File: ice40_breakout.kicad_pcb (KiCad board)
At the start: 4 copper layers, 80 x 100 mm, 224 parts, among them J1 Conn_01x10, J2 Conn_01x08, J3 Conn_01x06, J4 Conn_01x08, J5 USB_B_Micro, J6 7-17 V IN, Q1 2N7002, Q1 DMP3099L-7, SW1 SW_Push, SW2 SW_Push, SW3 SW_Push, SW4 SW_Push, SW5 SW_Push, SW6 SW_Push, SW7 JS202011SCQN, SW8 JS202011SCQN, SW9 JS202011SCQN, U1 ICE40HX4K-TQ144, U10 MAX40200AUK, U11 TXS0108EPW, U12 MAX40200AUK, U12 TPS562201, U13 TXS0108EPW, U14 MIC5365-3.3YC5, U15 MAX40200AUK, U2 IS61WV5128EDBLL-10TLI, U3 93LCxxBT-I_OT, U4 FT2232H, U5 IS25LP080D, U6 TLV62568APDRLR, U7 TLV62568APDRLR, U8 TXS0108EPW, U9 TXS0108EPW, Y1 ECS-3225S33-120-FN-TR, Y2 ECS-3225S33-500-FN-TR

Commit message: Continued on Power PCB design
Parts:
- moved C2 112.4 mm to (128.5, 63.6), turned to 90 degrees
- moved R14 103.2 mm to (127.0, 63.6), turned to 90 degrees
- moved R15 101.7 mm to (125.5, 63.6), turned to 270 degrees
- moved U6 95.4 mm to (123.5, 63.5), turned to 270 degrees
- moved C4 49.4 mm to (123.5, 67.8)
- moved C3 46.5 mm to (123.5, 66.2)
- moved C1 46.1 mm to (123.5, 61.2)
- moved L1 42.6 mm to (120.5, 65.2), turned to 270 degrees
- moved L2 26.6 mm to (126.2, 56.5), turned to 0 degrees
- moved C5 24.6 mm to (122.2, 53.5), turned to 90 degrees
- moved U7 23.3 mm to (124.5, 53.5), turned to 0 degrees
- moved C7 22.2 mm to (127.2, 53.5), turned to 90 degrees
- moved C8 21.9 mm to (128.8, 53.5), turned to 90 degrees
- moved R17 20.6 mm to (124.6, 51.5), turned to 0 degrees
- moved R16 18.7 mm to (124.6, 50.0), turned to 180 degrees
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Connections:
- net Net-(C34-Pad1) renamed /power/V_IN_FILTERED
- net Net-(C34-Pad2) renamed /power/GND_IN_FILTERED
- net Net-(C36-Pad1) renamed /power/V_IN_CHOKE
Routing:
- net /power/5V_IN: track 0.00 -> 27.6 mm
- net /power/V_IN_CHOKE: track 0.00 -> 11.5 mm
- net /power/V_IN: track 0.00 -> 8.98 mm
- net /power/GND_IN: track 0.00 -> 8.95 mm
- net +1V2: track 0.00 -> 8.01 mm, vias 0 -> 2
- net Net-(C43-Pad1): track 0.00 -> 6.06 mm
- net /power/FB_5V: track 0.05 -> 5.61 mm
- net /power/FB_1V2: track 0.00 -> 4.53 mm
- net Net-(C43-Pad2): track 0.00 -> 2.05 mm
- net GND: track 0.85 -> 2.85 mm, vias 11 -> 27
- net PG: track 1.10 -> 2.22 mm, vias 1 -> 2
- net /power/EN_HIGH_VOLTAGE: track 0.00 -> 1.05 mm, vias 0 -> 1
- net /power/EN_LOW_VOLTAGE: track 0.75 -> 1.50 mm, vias 1 -> 2
- net /power/V_IN_FILTERED: vias 0 -> 3
- net /power/GND_IN_FILTERED: vias 0 -> 3
- added copper zone on F.Cu, net +1V2
- added copper zone on F.Cu, net /power/5V_IN
- added copper zone on B.Cu, net /power/GND_IN_FILTERED
- added copper zone on F.Cu, net /power/GND_IN_FILTERED
- added copper zone on B.Cu, net /power/V_IN_FILTERED
- added copper zone on F.Cu, net /power/V_IN_FILTERED
- added copper zone on F.Cu, net /power/V_IN_PROTECTED
- added copper zone on F.Cu, net Net-(C43-Pad1)
- added copper zone on F.Cu, net Net-(L1-Pad1)
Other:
- net class V_IN added: clearance 0.2, trace_width 1, via_dia 0.6, via_drill 0.3

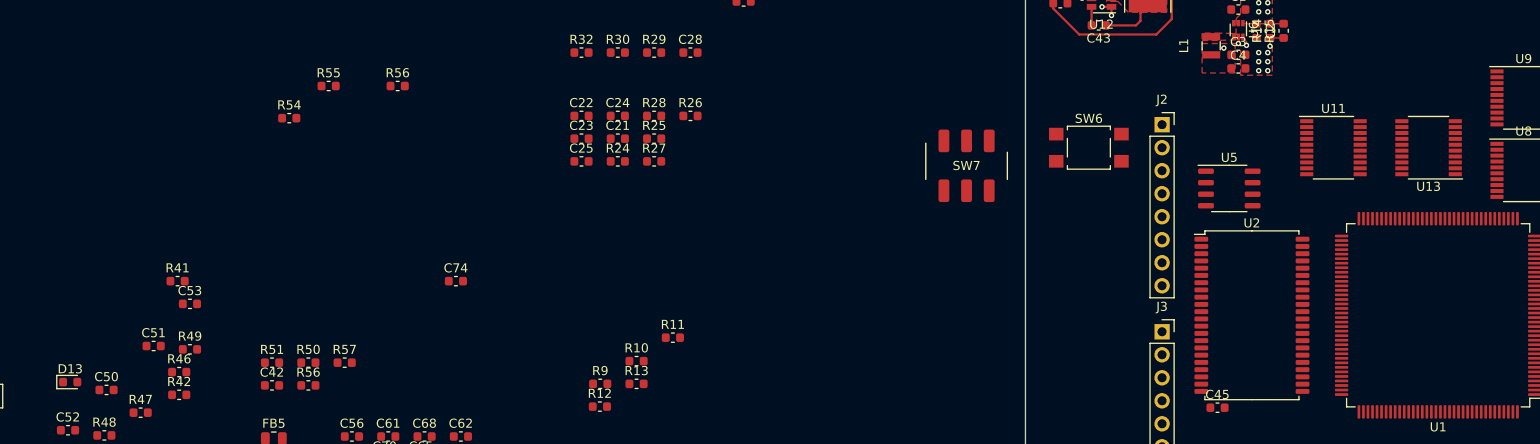
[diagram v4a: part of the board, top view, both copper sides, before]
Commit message: Implemented proper Powerseparation between FTDI and FPGA. The old solution may not work correctly
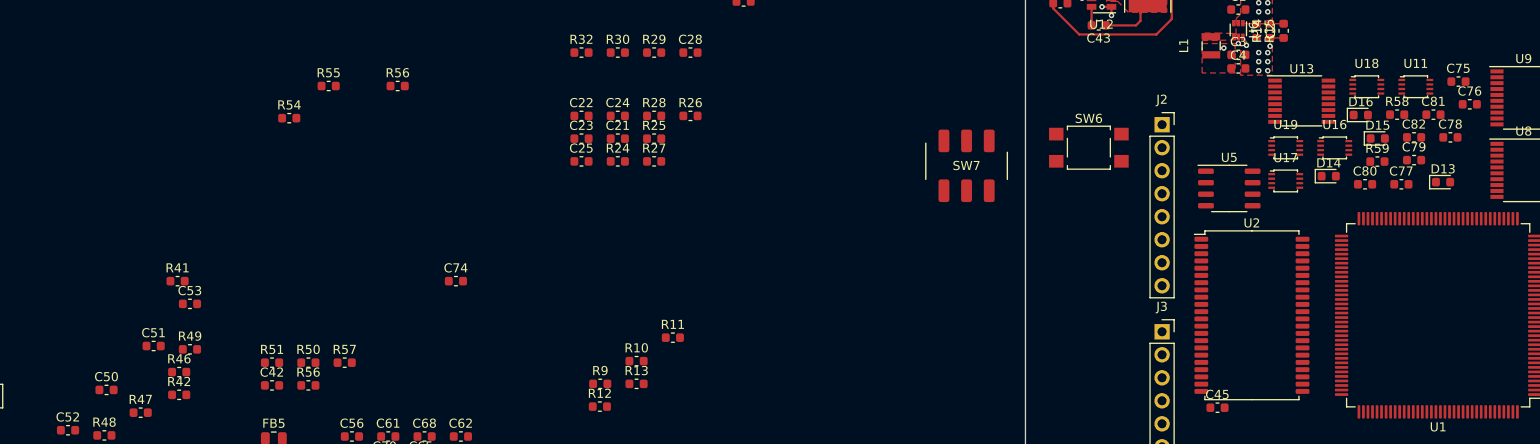
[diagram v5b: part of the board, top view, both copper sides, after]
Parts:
- added C75: 100nF, Capacitor_SMD:C_0603_1608Metric, F.Cu at (147.8, 69.2)
- added C76: 100nF, Capacitor_SMD:C_0603_1608Metric, F.Cu at (149.1, 71.7)
- added C77: 100nF, Capacitor_SMD:C_0603_1608Metric, F.Cu at (141.5, 80.5)
- added C78: 100nF, Capacitor_SMD:C_0603_1608Metric, F.Cu at (146.9, 75.4)
- added C79: 100nF, Capacitor_SMD:C_0603_1608Metric, F.Cu at (142.9, 77.9)
- added C80: 100nF, Capacitor_SMD:C_0603_1608Metric, F.Cu at (137.5, 80.5)
- added C81: 100nF, Capacitor_SMD:C_0603_1608Metric, F.Cu at (145.0, 72.8)
- added C82: 100nF, Capacitor_SMD:C_0603_1608Metric, F.Cu at (142.9, 75.4)
- added D14: CDBU5020, Diode_SMD:D_0603_1608Metric, F.Cu at (133.5, 79.6)
- added D15: CDBU5020, Diode_SMD:D_0603_1608Metric, F.Cu at (138.9, 75.5)
- added D16: CDBU5020, Diode_SMD:D_0603_1608Metric, F.Cu at (137.0, 72.9)
- added R58: 10k, Resistor_SMD:R_0603_1608Metric, F.Cu at (141.0, 72.8)
- added R59: 10k, Resistor_SMD:R_0603_1608Metric, F.Cu at (138.8, 78.0)
- added U16: SN74LVC2T45DCUR, Package_SO:VSSOP-8_2.4x2.1mm_P0.5mm, F.Cu at (134.1, 76.5)
- added U17: SN74LVC2T45DCUR, Package_SO:VSSOP-8_2.4x2.1mm_P0.5mm, F.Cu at (128.7, 80.2)
- added U18: SN74LVC2T45DCUR, Package_SO:VSSOP-8_2.4x2.1mm_P0.5mm, F.Cu at (137.7, 69.8)
- added U19: SN74LVC2T45DCUR, Package_SO:VSSOP-8_2.4x2.1mm_P0.5mm, F.Cu at (128.7, 76.5)
- U11: value TXS0108EPW -> SN74LVC2T45DCUR; footprint Package_SO:TSSOP-20_4.4x6.5mm_P0.65mm -> Package_SO:VSSOP-8_2.4x2.1mm_P0.5mm
- U13: value TXS0108EPW -> SN74AXC4T245PWR; footprint Package_SO:TSSOP-20_4.4x6.5mm_P0.65mm -> Package_SO:TSSOP-16_4.4x5mm_P0.65mm
- moved D13 153.1 mm to (146.1, 80.3)
- moved U13 14.9 mm to (130.5, 71.4), turned to 0 degrees
- moved U11 11.3 mm to (143.1, 69.8)
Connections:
- U11 pad 1: Net-(U11-Pad1) -> +3V3_FTDI
- U11 pad 2: +3V3_FTDI -> /USB Programmer/FTDI_MISO
- U11 pad 3: Net-(U11-Pad3) -> /USB Programmer/FTDI_CDONE
- U11 pad 4: Net-(U11-Pad4) -> GND
- U11 pad 5: Net-(U11-Pad5) -> GND
- U11 pad 6: Net-(U11-Pad6) -> CDONE
- U11 pad 7: Net-(U11-Pad7) -> /USB Programmer/MISO
- U11 pad 8: Net-(U11-Pad8) -> +3V3
- U13 pad 1: Net-(U13-Pad1) -> +3V3_FTDI
- U13 pad 10: +3V3_FTDI -> (no net)
- U13 pad 11: GND -> Net-(D16-Pad1)
- U13 pad 12: ICE_CLK_12M -> /USB Programmer/SS
- U13 pad 13: Net-(U13-Pad13) -> /USB Programmer/SCK
- U13 pad 14: Net-(U13-Pad14) -> Net-(D14-Pad2)
- U13 pad 15: ~DCD~ -> Net-(D14-Pad2)
- U13 pad 16: ~DSR~ -> +3V3
- U13 pad 3: Net-(U13-Pad3) -> +3V3_FTDI
- U13 pad 4: Net-(U13-Pad4) -> /USB Programmer/FTDI_SCK
- U13 pad 5: Net-(U13-Pad5) -> /USB Programmer/FTDI_MOSI
- U13 pad 6: Net-(U13-Pad6) -> /USB Programmer/FTDI_SS
- U13 pad 7: Net-(U13-Pad7) -> /USB Programmer/FTDI_CRESET_B
- U13 pad 8: Net-(U13-Pad8) -> GND
- U13 pad 9: /USB Programmer/12_MHZ -> GND
- U4 pad 16: Net-(U11-Pad1) -> /USB Programmer/FTDI_SCK
- U4 pad 17: Net-(U11-Pad3) -> /USB Programmer/FTDI_MOSI
- U4 pad 18: Net-(U11-Pad4) -> /USB Programmer/FTDI_MISO
- U4 pad 21: Net-(U11-Pad5) -> /USB Programmer/FTDI_SS
- U4 pad 23: Net-(U11-Pad6) -> /USB Programmer/FTDI_CDONE
- U4 pad 24: Net-(U11-Pad7) -> /USB Programmer/FTDI_CRESET_B
- U4 pad 38: Net-(U11-Pad8) -> /USB Programmer/FTDI_TXD
- U4 pad 39: Net-(U11-Pad9) -> /USB Programmer/FTDI_RXD
- U4 pad 40: Net-(U13-Pad1) -> /USB Programmer/~FTDI_RTS~
- U4 pad 41: Net-(U13-Pad3) -> /USB Programmer/~FTDI_CTS~
- U4 pad 43: Net-(U13-Pad4) -> /USB Programmer/~FTDI_DTR~
- U4 pad 44: Net-(U13-Pad5) -> /USB Programmer/~FTDI_DSR~
- U4 pad 45: Net-(U13-Pad6) -> /USB Programmer/~FTDI_DCD~

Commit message: Continued on routing
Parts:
- removed the C34 at (60.2, 113.0)
- removed the C35 at (51.0, 122.5)
- removed the C36 at (55.0, 120.0)
- removed the C37 at (59.0, 115.5)
- removed the C38 at (64.2, 113.0)
- removed the C41 at (63.0, 115.5)
- removed the C42 at (59.0, 120.5)
- removed the C43 at (68.2, 113.0)
- removed the C44 at (63.0, 118.0)
- removed the Q1 at (53.2, 134.5)
- removed the R35 at (49.0, 144.1)
- removed the R35 at (207.0, 45.4)
- removed the R36 at (211.1, 42.8)
- removed the R37 at (215.1, 40.3)
- removed the R40 at (215.1, 42.8)
- removed the R41 at (207.0, 50.5)
- removed the R42 at (219.1, 40.3)
- removed the R45 at (215.0, 45.3)
- removed the R46 at (219.1, 42.8)
- removed the R47 at (211.0, 50.5)
- removed the R48 at (223.1, 40.3)
- removed the R49 at (215.0, 47.8)
- removed the R50 at (219.0, 45.3)
- removed the R51 at (223.1, 42.8)
- removed the R56 at (30.7, 69.7)
- removed the U12 at (35.5, 142.7)
- removed the U15 at (40.4, 142.7)
- C32, C33, FB4: moved to B.Cu
- moved JP1 158.3 mm to (134.5, 47.0), turned to 270 degrees
- moved C71 154.2 mm to (159.8, 56.5), turned to 90 degrees
- moved C60 148.3 mm to (152.8, 60.0)
- moved FB4 146.8 mm to (150.5, 50.5)
- moved C47 146.2 mm to (161.0, 47.5), turned to 270 degrees
- moved R48 145.4 mm to (131.5, 50.0), turned to 180 degrees
- moved C72 139.1 mm to (140.8, 46.2), turned to 90 degrees
- moved C46 137.4 mm to (158.5, 50.0)
- moved C59 136.9 mm to (152.8, 61.5)
- moved C63 133.1 mm to (152.8, 55.5)
- moved C58 131.7 mm to (144.2, 68.2), turned to 270 degrees
- moved R37 130.7 mm to (152.8, 58.5)
- moved R36 130.0 mm to (152.8, 57.0), turned to 180 degrees
- moved C57 129.7 mm to (134.8, 62.8), turned to 180 degrees
- moved C69 128.0 mm to (143.0, 81.0), turned to 270 degrees
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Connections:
- D10 pad 3: Net-(D10-Pad3) -> (no net)
- D10 pad 4: Net-(D10-Pad4) -> (no net)
- J1 pad 3: Net-(J1-Pad3) -> (no net)
- J2 pad 1: Net-(J2-Pad1) -> (no net)
- J2 pad 2: Net-(J2-Pad2) -> (no net)
- J2 pad 3: /Header/INO_RESET -> (no net)
- J2 pad 4: /Header/INO_3V3 -> (no net)
- J2 pad 5: /Header/INO_5V -> (no net)
- J2 pad 8: Net-(J2-Pad8) -> (no net)
- J3 pad 1: /Header/INO_A0 -> (no net)
- J3 pad 2: /Header/INO_A1 -> (no net)
- J3 pad 3: /Header/INO_A2 -> (no net)
- J3 pad 4: /Header/INO_A3 -> (no net)
- J3 pad 5: /Header/INO_A4 -> (no net)
- J3 pad 6: /Header/INO_A5 -> (no net)
- J5 pad 4: Net-(J5-Pad4) -> (no net)
- SW7 pad 3: Net-(SW7-Pad3) -> (no net)
- SW7 pad 6: Net-(SW7-Pad6) -> (no net)
- SW8 pad 3: Net-(SW8-Pad3) -> (no net)
- SW8 pad 4: Net-(SW8-Pad4) -> (no net)
- SW8 pad 5: Net-(SW8-Pad5) -> (no net)
- SW8 pad 6: Net-(SW8-Pad6) -> (no net)
- SW9 pad 3: Net-(SW9-Pad3) -> (no net)
- SW9 pad 4: Net-(SW9-Pad4) -> (no net)
- SW9 pad 5: Net-(SW9-Pad5) -> (no net)
- SW9 pad 6: Net-(SW9-Pad6) -> (no net)
- U1 pad 109: Net-(U1-Pad109) -> (no net)
- U1 pad 120: Net-(U1-Pad120) -> (no net)
- U1 pad 121: Net-(U1-Pad121) -> (no net)
- U1 pad 135: Net-(U1-Pad135) -> (no net)
- U1 pad 22: Net-(U1-Pad22) -> (no net)
- U1 pad 23: Net-(U1-Pad23) -> (no net)
- U1 pad 63: Net-(U1-Pad63) -> (no net)
- U1 pad 64: Net-(U1-Pad64) -> (no net)
- U10 pad 4: Net-(U10-Pad4) -> (no net)
- U11 pad 2: /USB Programmer/FTDI_MISO -> /USB Programmer/FTDI_CDONE
- U11 pad 3: /USB Programmer/FTDI_CDONE -> /USB Programmer/FTDI_MISO
- U11 pad 6: CDONE -> /USB Programmer/MISO
- U11 pad 7: /USB Programmer/MISO -> CDONE
- U13 pad 10: (no net) -> /USB Programmer/SCK
- U13 pad 11: Net-(D16-Pad1) -> /USB Programmer/MOSI
- U13 pad 13: /USB Programmer/SCK -> Net-(D16-Pad1)
- U13 pad 4: /USB Programmer/FTDI_SCK -> /USB Programmer/FTDI_CRESET_B
- U13 pad 5: /USB Programmer/FTDI_MOSI -> /USB Programmer/FTDI_SS
- U13 pad 6: /USB Programmer/FTDI_SS -> /USB Programmer/FTDI_MOSI
- U13 pad 7: /USB Programmer/FTDI_CRESET_B -> /USB Programmer/FTDI_SCK
- U14 pad 4: Net-(U14-Pad4) -> (no net)
- U15 pad 4: Net-(U15-Pad4) -> (no net)
- U16 pad 2: /USB Programmer/FTDI_TXD -> /USB Programmer/~FTDI_RTS~
- U16 pad 3: /USB Programmer/~FTDI_RTS~ -> /USB Programmer/FTDI_TXD
- U16 pad 6: ~RTS~ -> TXD
- U16 pad 7: TXD -> ~RTS~
- U17 pad 2: /USB Programmer/~FTDI_DTR~ -> /USB Programmer/12_MHZ
- U17 pad 3: /USB Programmer/12_MHZ -> /USB Programmer/~FTDI_DTR~
- U17 pad 6: ICE_CLK_12M -> ~DTR~
- U17 pad 7: ~DTR~ -> ICE_CLK_12M
- U18 pad 2: /USB Programmer/~FTDI_DSR~ -> /USB Programmer/~FTDI_DCD~
- U18 pad 3: /USB Programmer/~FTDI_DCD~ -> /USB Programmer/~FTDI_DSR~
- U18 pad 6: ~DCD~ -> ~DSR~
- U18 pad 7: ~DSR~ -> ~DCD~
- U19 pad 2: /USB Programmer/FTDI_RXD -> /USB Programmer/~FTDI_CTS~
- U19 pad 3: /USB Programmer/~FTDI_CTS~ -> /USB Programmer/FTDI_RXD
- U19 pad 6: ~CTS~ -> RXD
- U19 pad 7: RXD -> ~CTS~
- U2 pad 1: Net-(U2-Pad1) -> (no net)
- U2 pad 2: Net-(U2-Pad2) -> (no net)
- U2 pad 21: Net-(U2-Pad21) -> (no net)
- U2 pad 22: Net-(U2-Pad22) -> (no net)
- U2 pad 23: Net-(U2-Pad23) -> (no net)
- U2 pad 24: Net-(U2-Pad24) -> (no net)
- U2 pad 25: Net-(U2-Pad25) -> (no net)
- U2 pad 42: Net-(U2-Pad42) -> (no net)
- U2 pad 43: Net-(U2-Pad43) -> (no net)
- U2 pad 44: Net-(U2-Pad44) -> (no net)
- U4 pad 19: Net-(U4-Pad19) -> (no net)
- U4 pad 22: Net-(U4-Pad22) -> (no net)
- U4 pad 26: Net-(U4-Pad26) -> (no net)
- U4 pad 27: Net-(U4-Pad27) -> (no net)
- U4 pad 28: Net-(U4-Pad28) -> (no net)
- U4 pad 29: Net-(U4-Pad29) -> (no net)
- U4 pad 3: Net-(U4-Pad3) -> (no net)
- U4 pad 30: Net-(U4-Pad30) -> (no net)
- U4 pad 32: Net-(U4-Pad32) -> (no net)
- U4 pad 33: Net-(U4-Pad33) -> (no net)
- U4 pad 34: Net-(U4-Pad34) -> (no net)
- U4 pad 36: Net-(U4-Pad36) -> (no net)
- U4 pad 46: Net-(U4-Pad46) -> (no net)
- U4 pad 48: Net-(U4-Pad48) -> (no net)
- U4 pad 52: Net-(U4-Pad52) -> (no net)
- U4 pad 53: Net-(U4-Pad53) -> (no net)
- U4 pad 57: Net-(U4-Pad57) -> (no net)
- U4 pad 58: Net-(U4-Pad58) -> (no net)
- U4 pad 60: Net-(U4-Pad60) -> (no net)
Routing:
- net +3V3_FTDI: track 0.00 -> 4.57 mm, vias 0 -> 3
- net VBUS: track 4.17 -> 6.94 mm
- added copper zone on In2.Cu, net +3V3_FTDI

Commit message: Continued on placing
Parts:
- C10, C11, C12, C13, C14, C15, C16, C17, C18, C19, C20, C42, C70, C74, C9, D13, R43, R44, R50, R51, R56, R57: moved to B.Cu
- moved C25 119.3 mm to (160.0, 126.5), turned to 270 degrees
- moved R28 115.6 mm to (161.5, 126.5), turned to 270 degrees
- moved C14 113.2 mm to (151.8, 103.8), turned to 180 degrees
- moved C20 111.9 mm to (152.8, 94.5), turned to 180 degrees
- moved C24 109.0 mm to (150.0, 126.5), turned to 270 degrees
- moved C17 108.8 mm to (152.8, 90.2), turned to 270 degrees
- moved C15 107.5 mm to (147.5, 104.0), turned to 90 degrees
- moved C10 107.4 mm to (138.5, 102.2)
- moved C16 106.7 mm to (143.8, 104.8), turned to 90 degrees
- moved C13 106.5 mm to (152.8, 93.0), turned to 180 degrees
- moved R27 104.4 mm to (151.5, 126.5), turned to 270 degrees
- moved C19 103.5 mm to (137.8, 104.8), turned to 90 degrees
- moved C23 102.6 mm to (140.0, 126.5), turned to 270 degrees
- moved C18 102.2 mm to (138.2, 98.2)
- moved R44 100.9 mm to (120.2, 84.2)
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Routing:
- net GND: track 2.85 -> 16.5 mm, vias 27 -> 36
- net +1V2: track 8.01 -> 13.7 mm, vias 2 -> 6
- added copper zone on B.Cu, net +1V2

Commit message: Continued with routing
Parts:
- added C83: 10 uF 6,3 V, Capacitor_SMD:C_0603_1608Metric, B.Cu at (145.0, 98.0)
- added C84: 10 uF 6,3 V, Capacitor_SMD:C_0603_1608Metric, F.Cu at (158.2, 110.0)
- added C85: 100nF, Capacitor_SMD:C_0603_1608Metric, B.Cu at (128.2, 97.5)
- added D17: DONE, LED_SMD:LED_0603_1608Metric, F.Cu at (109.0, 70.5)
- added Q2: Q_NMOS_GSD, Package_TO_SOT_SMD:SOT-23, F.Cu at (114.0, 68.5)
- added R60: 560, Resistor_SMD:R_0603_1608Metric, F.Cu at (109.0, 67.5)
- C26, C27, C28, C29, C30, C31, C45, C50, C51, C52, C53, C64, C65, C73, FB5, R31, R32, R41, R42, Y2: moved to B.Cu
- moved C29 105.7 mm to (157.5, 79.2), turned to 180 degrees
- moved R32 102.0 mm to (152.5, 76.2)
- moved C55 97.3 mm to (152.8, 54.0)
- moved FB5 96.3 mm to (142.2, 53.8), turned to 180 degrees
- moved R39 95.9 mm to (121.0, 78.5), turned to 270 degrees
- moved C28 94.6 mm to (157.5, 71.2), turned to 180 degrees
- moved R38 92.7 mm to (119.5, 78.5), turned to 270 degrees
- moved C52 92.4 mm to (145.8, 104.2)
- moved R20 91.5 mm to (163.0, 52.0), turned to 180 degrees
- moved C50 88.0 mm to (146.8, 90.8)
- moved R22 87.7 mm to (163.0, 53.5), turned to 180 degrees
- moved R31 87.7 mm to (152.5, 84.2)
- moved R21 87.1 mm to (163.0, 50.5), turned to 180 degrees
- moved C30 86.9 mm to (142.5, 57.9), turned to 180 degrees
- moved C31 84.5 mm to (142.5, 56.4), turned to 180 degrees
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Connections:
- SW7 pad 1: /power/EN_HIGH_VOLTAGE -> /power/EN_LOW_VOLTAGE
- SW7 pad 4: /power/EN_LOW_VOLTAGE -> /power/EN_HIGH_VOLTAGE
- U1 pad 101: /SRAM Memory/IO4 -> /SRAM Memory/A10
- U1 pad 102: /SRAM Memory/IO5 -> /SRAM Memory/A5
- U1 pad 104: /SRAM Memory/IO6 -> /SRAM Memory/A6
- U1 pad 105: /SRAM Memory/IO7 -> /SRAM Memory/A7
- U1 pad 106: ~SRAM_OE~ -> /SRAM Memory/A8
- U1 pad 107: ~SRAM_WE~ -> /SRAM Memory/A9
- U1 pad 79: /SRAM Memory/A5 -> /SRAM Memory/A18
- U1 pad 80: /SRAM Memory/A6 -> /SRAM Memory/IO0
- U1 pad 81: /SRAM Memory/A7 -> /SRAM Memory/A17
- U1 pad 82: /SRAM Memory/A8 -> /SRAM Memory/IO1
- U1 pad 83: /SRAM Memory/A9 -> /SRAM Memory/A16
- U1 pad 84: /SRAM Memory/A10 -> /SRAM Memory/IO2
- U1 pad 85: /SRAM Memory/A11 -> /SRAM Memory/A15
- U1 pad 87: /SRAM Memory/A12 -> ~SRAM_OE~
- U1 pad 88: /SRAM Memory/A13 -> /SRAM Memory/IO7
- U1 pad 90: /SRAM Memory/A14 -> /SRAM Memory/IO6
- U1 pad 91: /SRAM Memory/A15 -> /SRAM Memory/IO3
- U1 pad 93: /SRAM Memory/A16 -> /SRAM Memory/IO5
- U1 pad 94: /SRAM Memory/A17 -> ~SRAM_WE~
- U1 pad 95: /SRAM Memory/A18 -> /SRAM Memory/IO4
- U1 pad 96: /SRAM Memory/IO0 -> /SRAM Memory/A14
- U1 pad 97: /SRAM Memory/IO1 -> /SRAM Memory/A13
- U1 pad 98: /SRAM Memory/IO2 -> /SRAM Memory/A12
- U1 pad 99: /SRAM Memory/IO3 -> /SRAM Memory/A11
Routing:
- net GND: track 16.5 -> 61.9 mm, vias 36 -> 71
- net ~SRAM_CE~: track 0.00 -> 36.7 mm
- net /SRAM Memory/IO2: track 0.00 -> 23.1 mm, vias 0 -> 2
- net /SRAM Memory/IO1: track 0.00 -> 22.3 mm, vias 0 -> 2
- net /User Interface/LED0: track 0.00 -> 22.0 mm
- net /SRAM Memory/A5: track 0.00 -> 21.1 mm
- net /SRAM Memory/A4: track 0.00 -> 20.8 mm
- net /SRAM Memory/A6: track 0.00 -> 20.6 mm
- net /User Interface/LED1: track 0.00 -> 20.6 mm
- net /SRAM Memory/A3: track 0.00 -> 20.4 mm
- net /SRAM Memory/A7: track 0.00 -> 20.4 mm
- net /SRAM Memory/A9: track 0.00 -> 20.4 mm
- net /SRAM Memory/A8: track 0.00 -> 20.3 mm
- net /SRAM Memory/A2: track 0.00 -> 19.9 mm
- net /SRAM Memory/A1: track 0.00 -> 19.8 mm
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- added copper zone on In2.Cu, net +3V3
